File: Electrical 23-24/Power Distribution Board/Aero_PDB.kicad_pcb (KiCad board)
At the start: 2 copper layers, 77.3 x 144.2 mm, 8 parts, among them J101 Conn_02x13_Top_Bottom

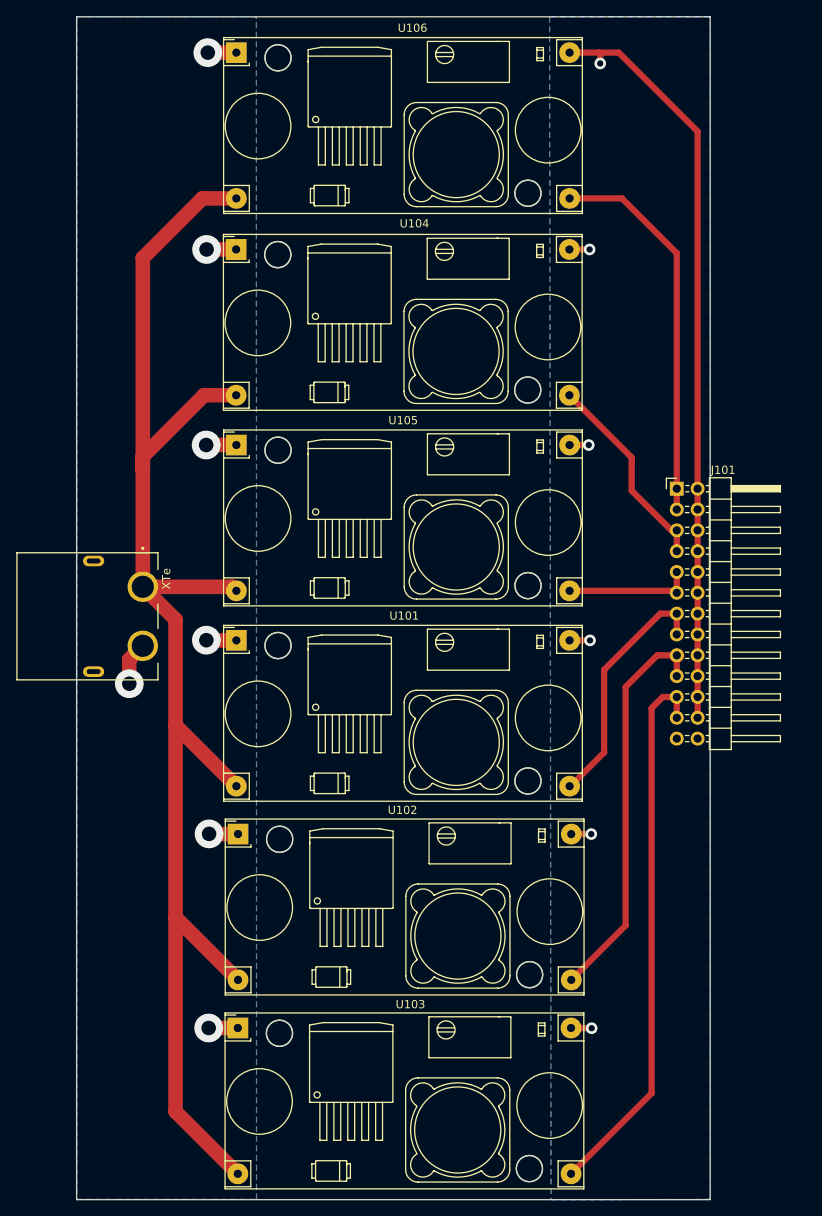
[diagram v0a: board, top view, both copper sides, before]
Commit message: Updates to the PDB Design
Pushed Some Buck Converters to the back 
Added more connectors (for RasPi, Bullet, etc.)
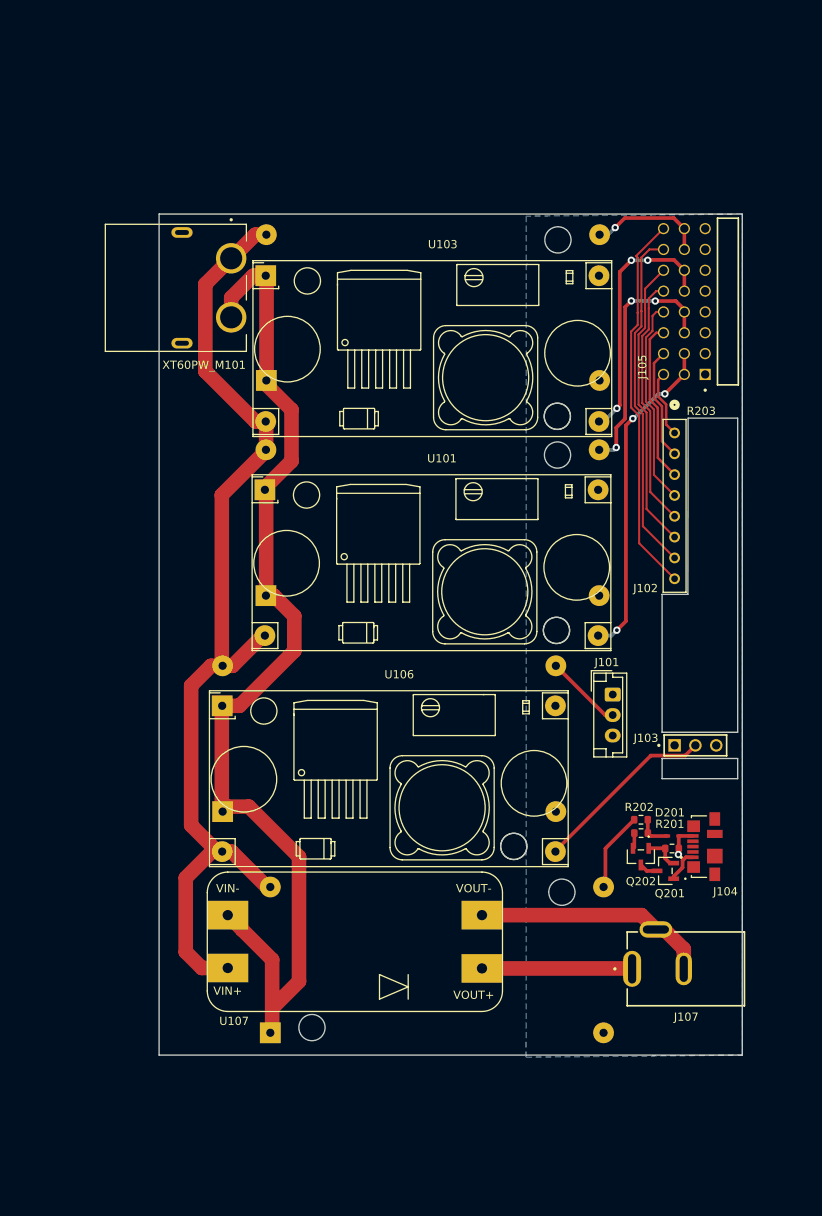
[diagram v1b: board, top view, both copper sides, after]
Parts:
- removed XTe: ~, Aero_PDB:AMASS_XT60PW-F
- added D201: 4.5V, Aero_PDB:SODFL1608X70N, F.Cu at (124.2, 128.4)
- added J102: Pixhawk Servo Conn, Aero_PDB:CONN8_LFBN-RC_SUL, F.Cu at (124.3, 79.2)
- added J103: Pixawk Backup Power, Aero_PDB:SAMTEC_DW-03-XX-X-S-XXX, F.Cu at (124.3, 117.3)
- added J104: USB_OTG, Aero_PDB:MOLEX_47346-0001, F.Cu at (129.2, 129.7)
- added J105: Servo to PDB Conn, Aero_PDB:SAMTEC_TSW-108-08-L-T-RA, F.Cu at (130.8, 63.2)
- added J107: DCJ200-10-A-XX-K_REVA, Aero_PDB:GCT_DCJ200-10-A-XX-K_REVA, F.Cu at (125.7, 144.6)
- added Q201: PNP, Aero_PDB:SOT-23-3_1P4X3P040_ONS, F.Cu at (123.2, 132.6)
- added Q202: PNP, Aero_PDB:SOT-23-3_1P4X3P040_ONS, F.Cu at (120.2, 130.9)
- added R201: 6.8k, Resistor_SMD:R_0603_1608Metric, F.Cu at (124.0, 129.9)
- added R202: 6.8k, Resistor_SMD:R_0603_1608Metric, F.Cu at (120.2, 128.0)
- added R203: 2.7k, Resistor_SMD:R_0603_1608Metric, F.Cu at (120.2, 126.4)
- added U107: ~, Aero_PDB:MT3608_module, F.Cu at (83.8, 141.3)
- added U108: ~, Aero_PDB:YAAJ_DCDC_StepDown_LM2596, B.Cu at (75.0, 152.4)
- added XT60PW_M101: ~, Aero_PDB:AMASS_XT60PW-F, F.Cu at (70.3, 61.5)
- J101: value Conn_02x13_Top_Bottom -> Gimbal Conn; footprint Connector_PinHeader_2.54mm:PinHeader_2x13_P2.54mm_Horizontal -> Connector_JST:JST_EH_B3B-EH-A_1x03_P2.50mm_Vertical
- U102, U104, U105: moved to B.Cu
- moved U103 91.8 mm to (74.5, 60.0)
- moved U106 79.7 mm to (69.2, 112.5)
- moved U105 44.7 mm to (69.2, 125.4)
- moved U102 29.3 mm to (74.5, 99.1)
- moved J101 26.3 mm to (116.8, 111.1), turned to -90 degrees
- moved U101 18.7 mm to (74.4, 86.2)
- moved U104 16.4 mm to (74.5, 72.8)
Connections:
- J101 pad 1: /Servo_1&2_PWR -> /Gimbal_Signal
- J101 pad 2: /GND_LV -> /Gimbal_Power
- J101 pad 3: /Servo_1&2_PWR -> GND
- U101 pad 1: /GND_HV -> GND
- U101 pad 3: /Servo_7&8_PWR -> /Servo_1&2_PWR
- U101 pad 4: /GND_LV -> GND
- U102 pad 1: /GND_HV -> GND
- U102 pad 3: /Pickhawk_PWR -> /Servo_3&4_PWR
- U102 pad 4: /GND_LV -> GND
- U103 pad 1: /GND_HV -> GND
- U103 pad 3: /Gimbal_Power -> /Servo_5&6_PWR
- U103 pad 4: /GND_LV -> GND
- U104 pad 1: /GND_HV -> GND
- U104 pad 3: /Servo_3&4_PWR -> /Servo_7&8_PWR
- U104 pad 4: /GND_LV -> GND
- U105 pad 1: /GND_HV -> GND
- U105 pad 3: /Servo_5&6_PWR -> /Gimbal_Power
- U105 pad 4: /GND_LV -> GND
- U106 pad 1: /GND_HV -> GND
- U106 pad 3: /Servo_1&2_PWR -> /Pickhawk_PWR
- U106 pad 4: /GND_LV -> GND
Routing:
- net GND: track 0.00 -> 135.4 mm, vias 0 -> 1
- net /GND_LV: track 105.1 -> 0.00 mm, vias 6 -> 0
- net /Gimbal_Power: track 67.0 -> 9.37 mm
- net /+12V: track 179.9 -> 124.6 mm
- net /Servo_8_Signal: track 0.00 -> 46.7 mm
- net /Servo_7_Signal: track 0.00 -> 42.1 mm
- net /Servo_6_Signal: track 0.00 -> 35.6 mm
- net /Servo_5_Signal: track 0.00 -> 30.7 mm
- net /Bullet_GND : track 0.00 -> 28.7 mm
- net /GND_HV: track 26.8 -> 0.00 mm, vias 7 -> 0
- net /Pickhawk_PWR: track 48.8 -> 22.5 mm
- net /Servo_4_Signal: track 0.00 -> 25.2 mm
- net /Servo_3_Signal: track 0.00 -> 19.8 mm
- net /Bullet_PWR: track 0.00 -> 18.3 mm
- net /Servo_7&8_PWR: track 30.4 -> 14.3 mm, vias 0 -> 1
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- added copper zone on B.Cu, net GND
- removed copper zone on B.Cu, net /GND_HV
- removed copper zone on B.Cu, net /GND_LV
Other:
- board size 77.3 x 144.2 mm -> 71.1 x 102.6 mm

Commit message: Final PDB (missing Aero Logo)
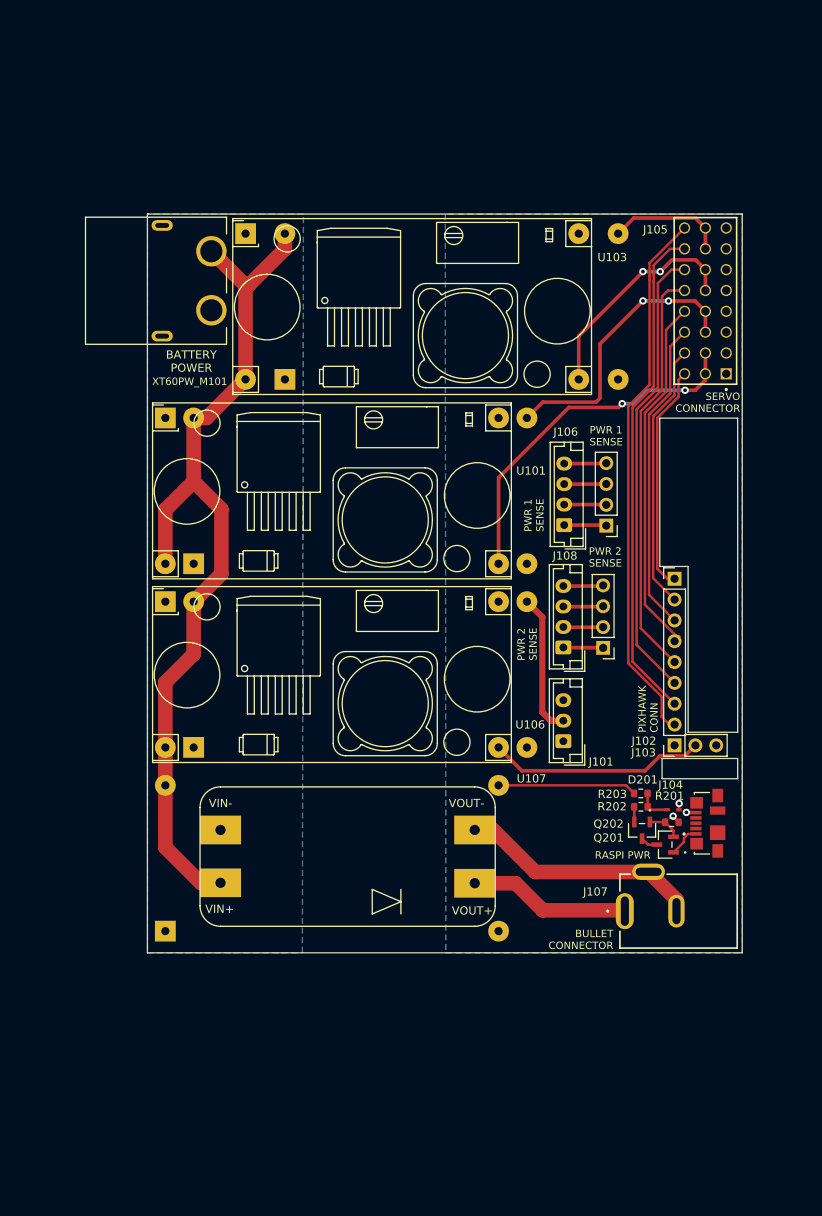
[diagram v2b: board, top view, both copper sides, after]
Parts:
- added J106: Conn_01x04_Pin, Connector_JST:JST_EH_B4B-EH-A_1x04_P2.50mm_Vertical, F.Cu at (110.9, 90.5)
- added J108: Conn_01x04_Pin, Connector_JST:JST_EH_B4B-EH-A_1x04_P2.50mm_Vertical, F.Cu at (110.8, 105.4)
- added PWR_SENSE_1: PinHeader_1x04_P2.54mm_Vertical, Connector_PinHeader_2.54mm:PinHeader_1x04_P2.54mm_Vertical, F.Cu at (115.6, 105.4)
- added PWR_SENSE_1: PinHeader_1x04_P2.54mm_Vertical, Connector_PinHeader_2.54mm:PinHeader_1x04_P2.54mm_Vertical, F.Cu at (116.0, 90.5)
- J102: footprint Aero_PDB:CONN8_LFBN-RC_SUL -> Connector_PinHeader_2.54mm:PinHeader_1x08_P2.54mm_Vertical
- J103: footprint Aero_PDB:SAMTEC_DW-03-XX-X-S-XXX -> Connector_PinHeader_2.54mm:PinHeader_1x03_P2.54mm_Vertical
- J105: footprint Aero_PDB:SAMTEC_TSW-108-08-L-T-RA -> Aero_PDB:SAMTEC_TSW-108-07-G-T
- moved U108 17.8 mm to (62.2, 140.0)
- moved J102 17.8 mm to (124.3, 97.0), turned to 0 degrees
- moved U101 15.0 mm to (62.2, 77.4)
- moved U106 14.5 mm to (62.2, 99.8)
- moved U107 10.4 mm to (83.0, 130.9)
- moved U102 9.63 mm to (65.7, 95.2)
- moved U105 8.58 mm to (65.7, 117.6)
- moved J101 8.28 mm to (110.8, 116.8), turned to 90 degrees
- moved J107 7.09 mm to (124.8, 137.5)
- moved U103 5.69 mm to (72.0, 54.9)
- moved Q202 3.21 mm to (120.4, 127.7)
- moved R202 3.21 mm to (120.2, 124.8)
- moved R203 3.21 mm to (120.2, 123.2)
- moved D201 3.21 mm to (124.1, 125.2)
- moved Q201 3.21 mm to (123.2, 129.4)
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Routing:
- net GND: track 135.4 -> 2.96 mm, vias 1 -> 3
- net /Servo_6_Signal: track 35.6 -> 55.7 mm
- net /Servo_5_Signal: track 30.7 -> 50.4 mm
- net /Servo_1_Signal: track 8.24 -> 27.7 mm
- net /Servo_8_Signal: track 46.7 -> 66.1 mm
- net /Servo_4_Signal: track 25.2 -> 44.4 mm
- net /Servo_7_Signal: track 42.1 -> 61.3 mm
- net /Servo_2_Signal: track 13.7 -> 32.7 mm
- net /Servo_3_Signal: track 19.8 -> 38.2 mm
- net /+12V: track 124.6 -> 110.7 mm
- net /Gimbal_Power: track 9.37 -> 17.3 mm
- net /Power Protection /RPI_PWR_IN: track 9.75 -> 16.9 mm
- net /I_1_Signal: track 0.00 -> 5.16 mm
- net /V_1_GND : track 0.00 -> 5.15 mm
- net /I_1_GND : track 0.00 -> 5.14 mm
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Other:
- board size 71.1 x 102.6 mm -> 72.5 x 90.1 mm
- board text added: "BATTERY POWER"
- board text added: "BULLET CONNECTOR"
- board text added: "PIXHAWK CONN"
- board text added: "PWR 1 SENSE"
- board text added: "PWR 2 SENSE"
- board text added: "RASPI PWR"
- board text added: "SERVO CONNECTOR"
- board text added: "Solomiia Kachur Ari Bobesh"

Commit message: Final Board
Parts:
- added G***: LOGO, LOGO, B.Cu at (118.0, 118.9)
- J101: footprint Connector_JST:JST_EH_B3B-EH-A_1x03_P2.50mm_Vertical -> Connector_JST:JST_XH_B3B-XH-A_1x03_P2.50mm_Vertical
- J106, J108: footprint Connector_JST:JST_EH_B4B-EH-A_1x04_P2.50mm_Vertical -> Connector_JST:JST_XH_B4B-XH-A_1x04_P2.50mm_Vertical
- moved PWR_SENSE_1 1.07 mm to (116.7, 105.4)
- moved J101 0.99 mm to (111.8, 116.8)
- moved PWR_SENSE_1 0.64 mm to (116.6, 90.4)
- moved J106 0.34 mm to (110.8, 90.1)
- moved J108 0.15 mm to (110.9, 105.4)
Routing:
- net /Gimbal_Power: track 17.3 -> 18.3 mm
- net /V_2_Signal: track 4.88 -> 5.83 mm
- net /I_2_GND : track 4.88 -> 5.82 mm
- net /V_2_GND : track 4.89 -> 5.83 mm
- net /I_2_Signal: track 4.87 -> 5.80 mm
- net /I_1_GND : track 5.14 -> 5.97 mm
- net /I_1_Signal: track 5.16 -> 5.94 mm
- net /V_1_Signal: track 5.14 -> 5.91 mm
- net /V_1_GND : track 5.15 -> 5.91 mm

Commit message: Finalize PDB board
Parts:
- removed PWR_SENSE_1 (x2): PinHeader_1x04_P2.54mm_Vertical, Connector_PinHeader_2.54mm:PinHeader_1x04_P2.54mm_Vertical
- added J1: Conn_01x04_Pin, Connector_PinHeader_2.54mm:PinHeader_1x04_P2.54mm_Vertical, F.Cu at (116.7, 105.4)
- added J2: Conn_01x04_Pin, Connector_PinHeader_2.54mm:PinHeader_1x04_P2.54mm_Vertical, F.Cu at (116.7, 90.4)
- added J3: RCIN, Connector_PinHeader_2.54mm:PinHeader_1x03_P2.54mm_Vertical, F.Cu at (105.9, 121.7)
- added J4: RCIN, Connector_PinHeader_2.54mm:PinHeader_1x03_P2.54mm_Vertical, F.Cu at (124.3, 119.9)
- D201: value 4.5V -> 5.1V; footprint Aero_PDB:SODFL1608X70N -> Aero_PDB:SOD1608X70
- J101: footprint Connector_JST:JST_XH_B3B-XH-A_1x03_P2.50mm_Vertical -> Connector_JST:JST_EH_B2B-EH-A_1x02_P2.50mm_Vertical
- J106, J108: value Conn_01x04_Pin -> JST_XH_4
- moved J107 15.3 mm to (109.8, 134.8), turned to 0 degrees
- moved R203 13.1 mm to (131.5, 129.9), turned to -90 degrees
- moved J104 12.6 mm to (127.8, 139.3), turned to 0 degrees
- moved R202 10.9 mm to (129.8, 130.0), turned to -90 degrees
- moved D201 10.2 mm to (129.5, 133.9), turned to -90 degrees
- moved R201 8.06 mm to (127.9, 133.7), turned to -90 degrees
- moved Q202 7.01 mm to (126.9, 130.1), turned to 90 degrees
- moved Q201 4.03 mm to (125.2, 132.9), turned to 0 degrees
- moved J101 2.54 mm to (111.7, 114.3)
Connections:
- J101 pad 1: /Gimbal_Signal -> /Gimbal_Power
- J101 pad 2: /Gimbal_Power -> GND
- J103 pad 3: GND2 -> GND
- J106 pad 1: /I_1_Signal -> /V_1_Signal
- J106 pad 2: /I_1_GND  -> /V_1_GND 
- J106 pad 3: /V_1_Signal -> /I_1_Signal
- J106 pad 4: /V_1_GND  -> /I_1_GND 
- J108 pad 1: /I_2_Signal -> /V_2_Signal
- J108 pad 2: /I_2_GND  -> /V_2_GND 
- J108 pad 3: /V_2_Signal -> /I_2_Signal
- J108 pad 4: /V_2_GND  -> /I_2_GND 
- Q201 pad 3: Net-(Q201-E) -> /Power Protection /RPI_PWR_IN
- Q202 pad 3: Net-(Q201-E) -> /Power Protection /RPI_PWR_IN
- U101 pad 1: GND -> GND1
- U102 pad 1: GND -> GND1
- U103 pad 1: GND -> GND1
- U104 pad 1: GND -> GND1
- U105 pad 1: GND -> GND1
- U106 pad 1: GND -> GND1
- U107 pad 2: GND -> GND1
- XT60PW_M101 pad 2: GND -> GND1
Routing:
- net /RCIN: track 0.00 -> 19.2 mm
- net /Power Protection /RPI_PWR_IN: track 16.9 -> 35.8 mm
- net /Bullet_PWR: track 19.7 -> 33.7 mm
- net /Bullet_GND : track 29.5 -> 18.9 mm
- net Net-(Q201-E): track 2.11 -> 0.00 mm
- net /Pickhawk_PWR: track 26.5 -> 25.7 mm
- added copper zone on B.Cu, net GND1
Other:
- board size 72.5 x 90.1 mm -> 72.6 x 89.9 mm

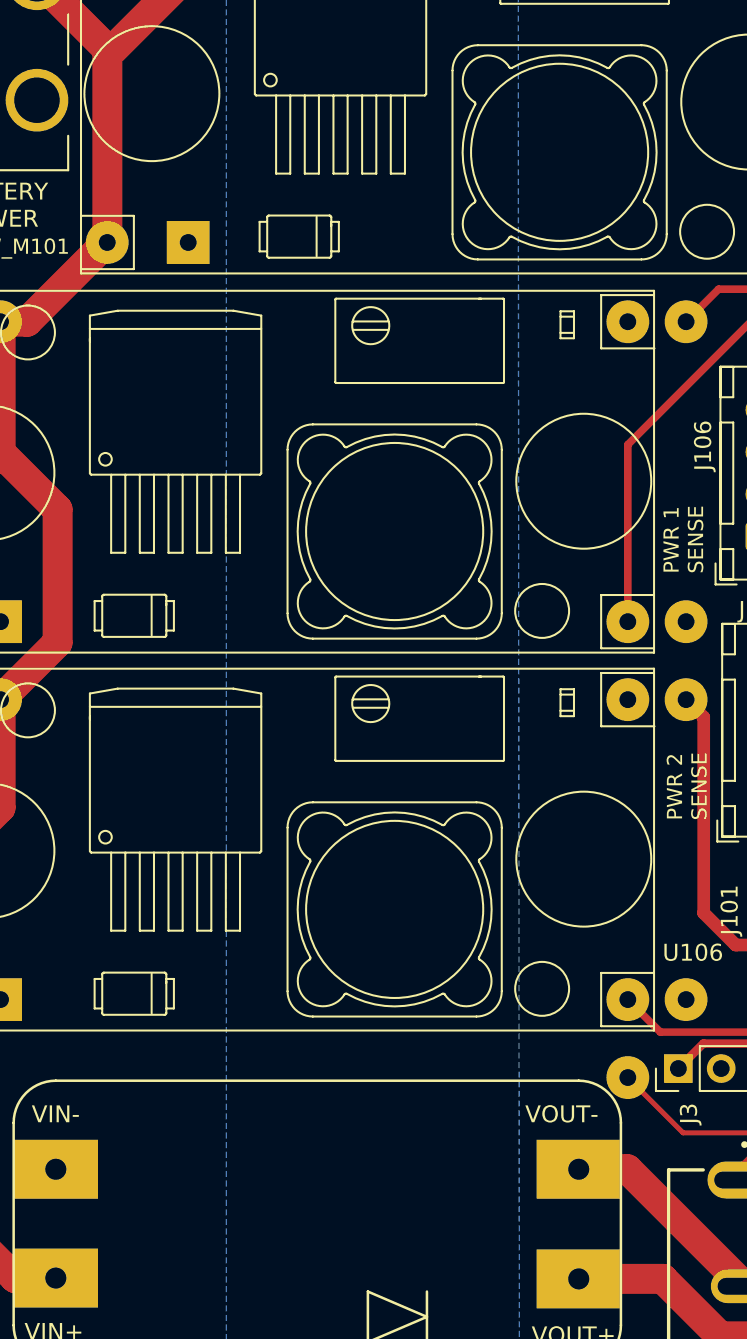
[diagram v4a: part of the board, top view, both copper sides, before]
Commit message: Add JLC Serial # Location to All
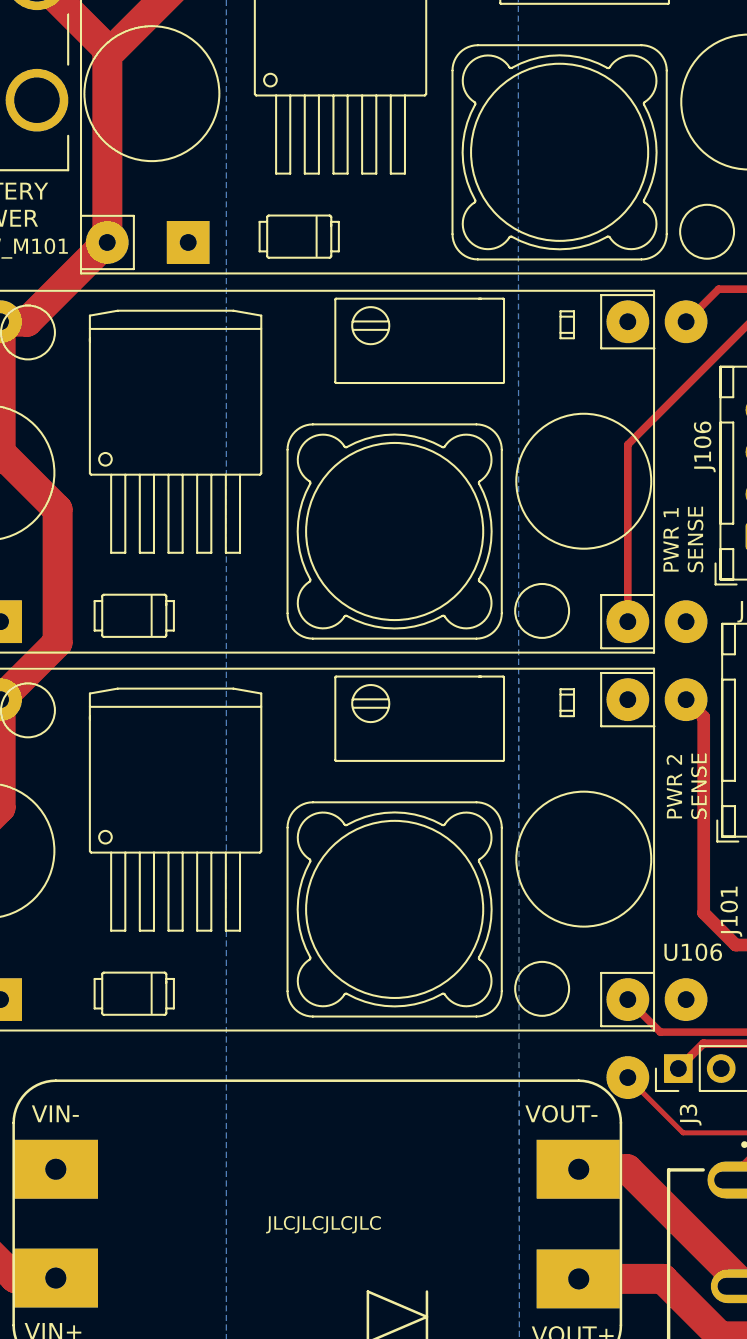
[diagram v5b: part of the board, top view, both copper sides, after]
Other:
- board text added: "JLCJLCJLCJLC"

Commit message: Changed USB micro to USB A
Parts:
- removed J104: USB_OTG, Aero_PDB:MOLEX_47346-0001
- added J113: USB_A, Aero_PDB:GCT_USB1130-15-A_REVA, F.Cu at (129.9, 131.8)
- D201: footprint Aero_PDB:SOD1608X70 -> Aero_PDB:SODFL1608X70N
- J101: footprint Connector_JST:JST_EH_B2B-EH-A_1x02_P2.50mm_Vertical -> Connector_JST:JST_XH_B2B-XH-A_1x02_P2.50mm_Vertical
- moved R203 11.3 mm to (120.4, 127.4), turned to 0 degrees
- moved R202 9.41 mm to (120.5, 129.0), turned to 0 degrees
- moved D201 6.82 mm to (124.4, 129.3), turned to 0 degrees
- moved Q202 6.59 mm to (120.6, 131.9), turned to 180 degrees
- moved R201 4.69 mm to (124.2, 130.9), turned to 0 degrees
- moved Q201 1.92 mm to (123.4, 133.6), turned to 90 degrees
- renumbered J107 to J106, J3 to J107, J106 to J109, J4 to J110, J1 to J111, J2 to J112
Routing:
- net /Power Protection /RPI_PWR_IN: track 35.8 -> 28.3 mm
- net /RPI_PWR: track 3.94 -> 3.11 mm

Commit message: Final board exports
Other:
- outline, holes or cut-outs redrawn
- board text added: "Power Distribution Board V1 04/19/2024"
